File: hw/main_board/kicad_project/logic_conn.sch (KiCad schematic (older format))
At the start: 11 parts, among them P6 CONN_20X2, U8 MAX3002, U9 MAX3002

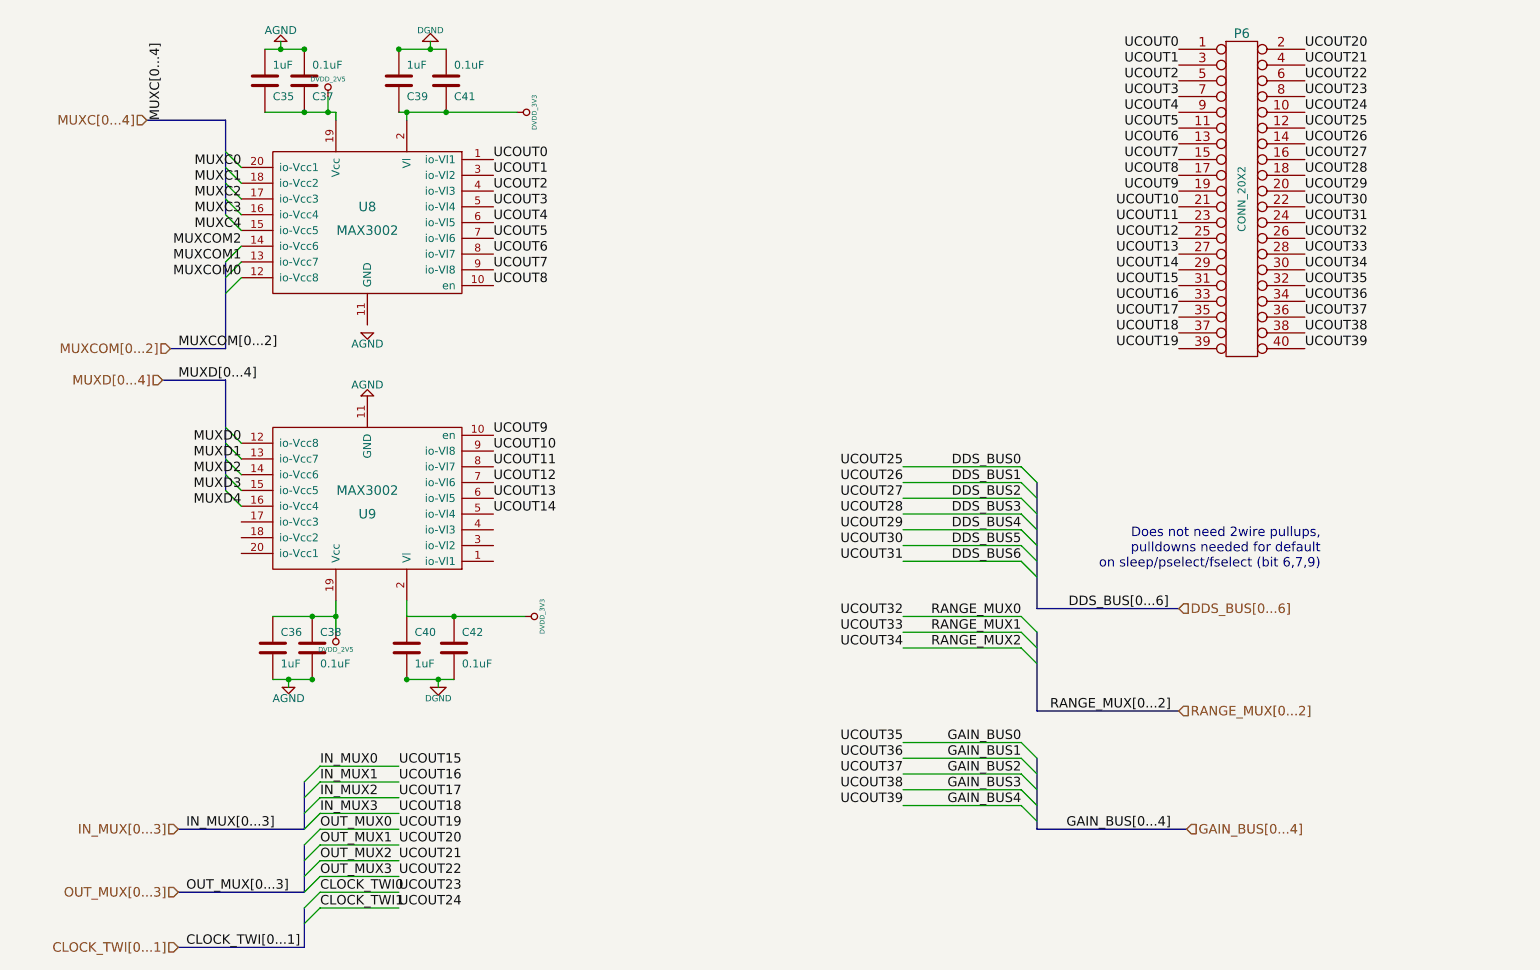
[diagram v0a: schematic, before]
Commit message: refactored schematic, finalized gain/range
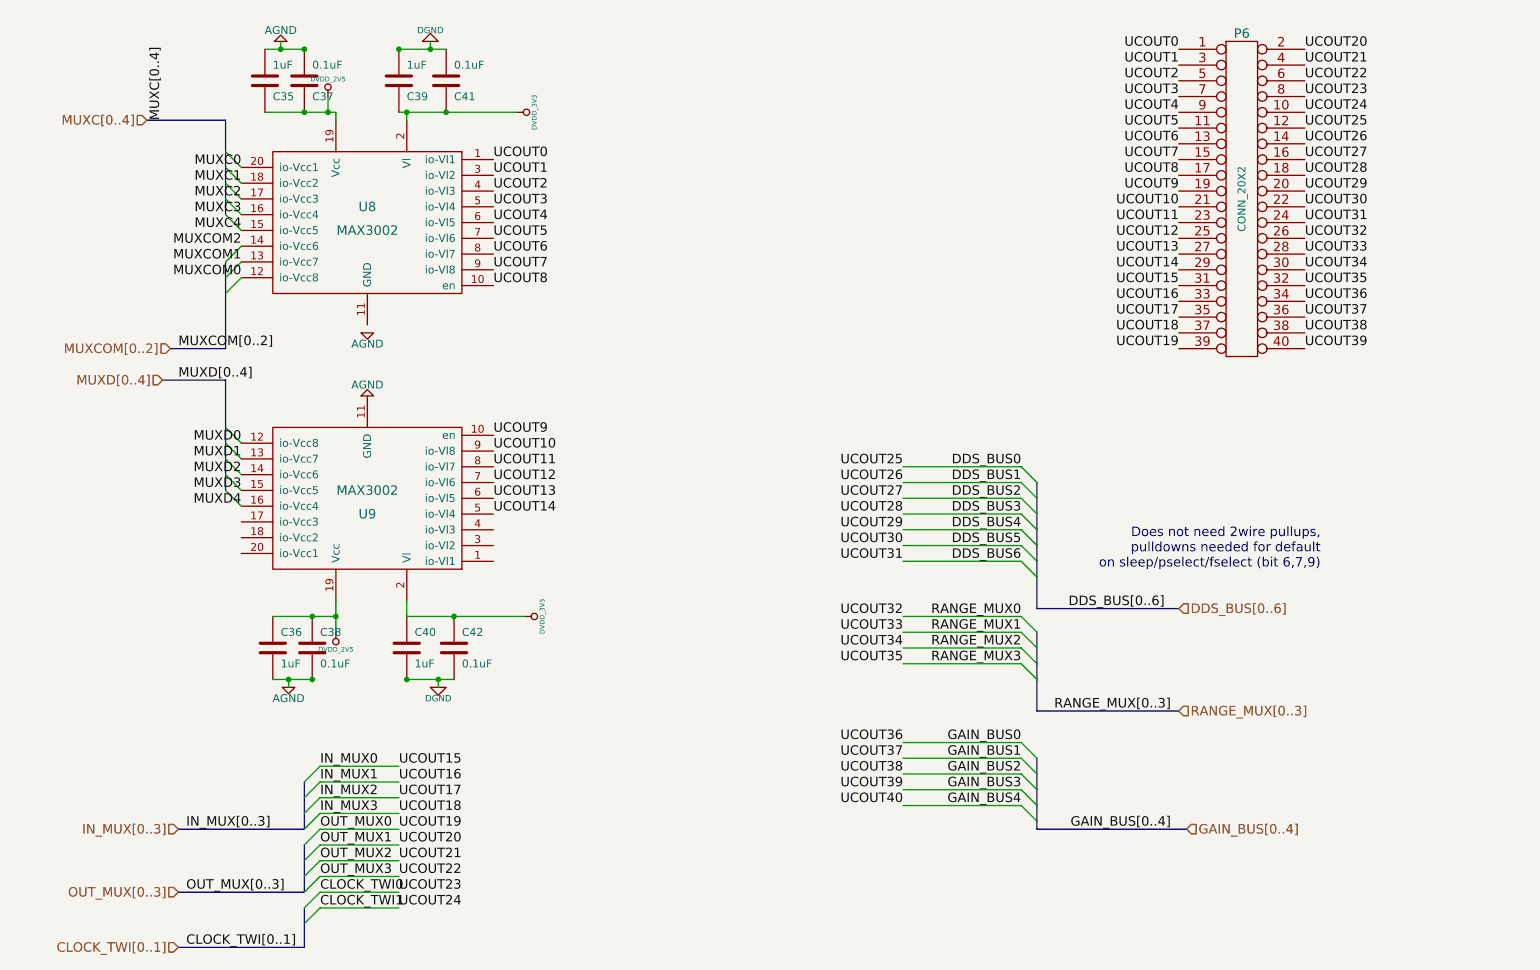
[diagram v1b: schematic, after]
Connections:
- net GAIN_BUS0: now also P6.34 (P34); no longer P6.32 (P32)
- net GAIN_BUS1: now also P6.36 (P36); no longer P6.34 (P34)
- net GAIN_BUS2: now also P6.38 (P38); no longer P6.36 (P36)
- net GAIN_BUS3: now also P6.40 (P40); no longer P6.38 (P38)
- net GAIN_BUS4: no longer P6.40 (P40)
- new net RANGE_MUX3: P6.32 (P32)
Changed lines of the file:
@@
 $Descr A4 11693 8268
 encoding utf-8
-Sheet 3 3
+Sheet 3 7
 Title ""
 Date "26 feb 2014"
@@
 $EndDescr
 Text Label 6900 5400 2    60   ~ 0
+UCOUT40
+Text Label 6900 5300 2    60   ~ 0
 UCOUT39
-Text Label 6900 5300 2    60   ~ 0
+Text Label 6900 5200 2    60   ~ 0
 UCOUT38
-Text Label 6900 5200 2    60   ~ 0
+Text Label 6900 5100 2    60   ~ 0
 UCOUT37
-Text Label 6900 5100 2    60   ~ 0
+Text Label 6900 5000 2    60   ~ 0
 UCOUT36
-Text Label 6900 5000 2    60   ~ 0
-UCOUT35
 Text Label 7650 5400 2    60   ~ 0
 GAIN_BUS4
@@
 GAIN_BUS0
 Text Label 8600 5550 2    60   ~ 0
-GAIN_BUS[0...4]
+GAIN_BUS[0..4]
 Text Label 8600 4800 2    60   ~ 0
-RANGE_MUX[0...2]
+RANGE_MUX[0..3]
 Wire Wire Line
 	7650 5400 6900 5400
@@
 DDS_BUS0
 Text Label 7950 4150 0    60   ~ 0
-DDS_BUS[0...6]
+DDS_BUS[0..6]
 Entry Wire Line
 	7650 3850 7750 3950
@@
 	7650 3250 7750 3350
 Text Label 2350 6300 0    60   ~ 0
-CLOCK_TWI[0...1]
+CLOCK_TWI[0..1]
 Text Label 2350 5950 0    60   ~ 0
-OUT_MUX[0...3]
+OUT_MUX[0..3]
 Text Label 3700 6050 0    60   ~ 0
 UCOUT24
@@
 IN_MUX0
 Text Label 2350 5550 0    60   ~ 0
-IN_MUX[0...3]
+IN_MUX[0..3]
 Entry Wire Line
 	3100 5450 3200 5350
@@
 UCOUT0
 Text Label 2300 2700 0    60   ~ 0
-MUXD[0...4]
+MUXD[0..4]
 Entry Wire Line
 	2600 3400 2700 3500
@@
 $EndComp
 Text Label 2300 2500 0    60   ~ 0
-MUXCOM[0...2]
+MUXCOM[0..2]
 Text Label 2200 1050 1    60   ~ 0
-MUXC[0...4]
+MUXC[0..4]
 $Comp
 L DVDD_3V3 #PWR047
@@
 Does not need 2wire pullups, \npulldowns needed for default\n on sleep/pselect/fselect (bit 6,7,9)
 Text HLabel 8650 4800 2    60   Input ~ 0
-RANGE_MUX[0...2]
+RANGE_MUX[0..3]
 Text HLabel 8700 5550 2    60   Input ~ 0
-GAIN_BUS[0...4]
+GAIN_BUS[0..4]
 Text HLabel 8650 4150 2    60   Input ~ 0
-DDS_BUS[0...6]
+DDS_BUS[0..6]
 Text HLabel 2300 5550 0    60   Input ~ 0
-IN_MUX[0...3]
+IN_MUX[0..3]
 Text HLabel 2300 5950 0    60   Input ~ 0
-OUT_MUX[0...3]
+OUT_MUX[0..3]
 Text HLabel 2300 6300 0    60   Input ~ 0
-CLOCK_TWI[0...1]
+CLOCK_TWI[0..1]
 Text HLabel 2100 1050 0    60   Input ~ 0
-MUXC[0...4]
+MUXC[0..4]
 Text HLabel 2250 2500 0    60   Input ~ 0
-MUXCOM[0...2]
+MUXCOM[0..2]
 Text HLabel 2200 2700 0    60   Input ~ 0
-MUXD[0...4]
+MUXD[0..4]
 $Comp
 L CONN_20X2 P6
@@
 Text Label 9450 2500 0    60   ~ 0
 UCOUT39
+Entry Wire Line
+	7650 4500 7750 4600
+Wire Wire Line
+	7650 4500 6900 4500
+Text Label 6900 4500 2    60   ~ 0
+UCOUT35
+Text Label 7650 4500 2    60   ~ 0
+RANGE_MUX3
 $EndSCHEMATC

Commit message: started mainboard pcb layout, fixing small things in schematic, TODO: schematic connector symbols and pads
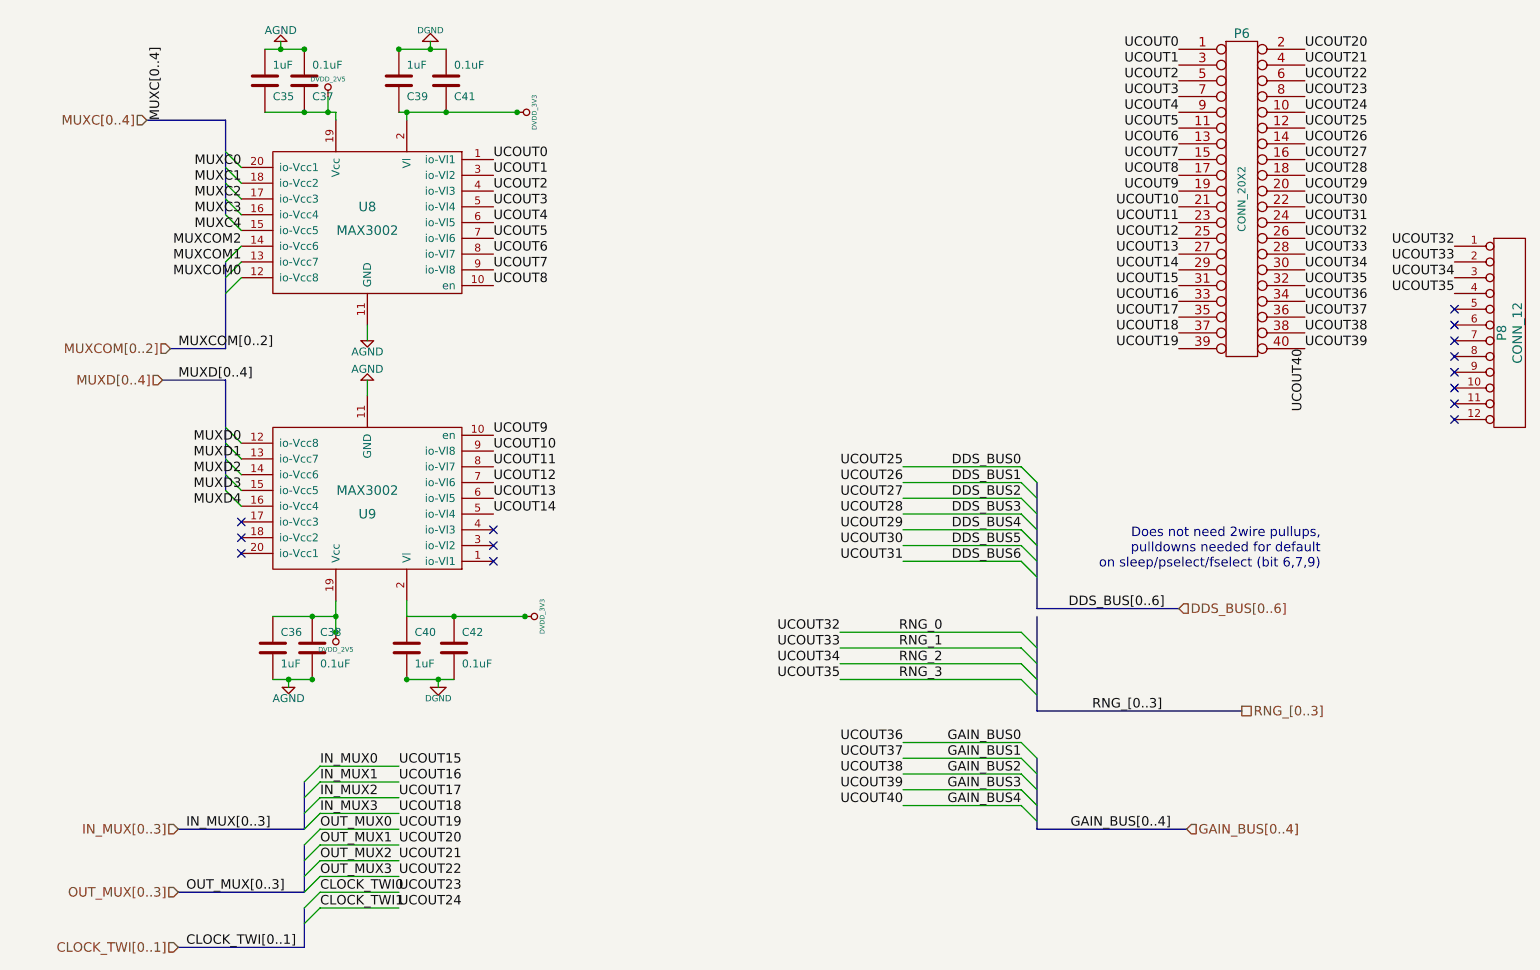
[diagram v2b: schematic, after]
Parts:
- added P8: CONN_12, symbol CONN_12
- C35, C36, C37, C38, C39, C40, C41, C42: footprint (none) -> 0603
- U8, U9: footprint (none) -> TSSOP_20
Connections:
- net AGND: now also U8.11 (GND)
- net RANGE_MUX0 renamed RNG_0
- net RNG_0: now also P8.1 (P1)
- net RANGE_MUX1 renamed RNG_1
- net RNG_1: now also P8.2 (P2)
- net RANGE_MUX2 renamed RNG_2
- net RNG_2: now also P8.3 (P3)
- net RANGE_MUX3 renamed RNG_3
- net RNG_3: now also P8.4 (P4)
- no-connect marks 0 -> 14
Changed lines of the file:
@@
 encoding utf-8
 Sheet 3 7
-Title ""
-Date "26 feb 2014"
-Rev ""
+Title "Microcontroller interface/translator"
+Date "01 Feb 2014"
+Rev "A"
 Comp ""
-Comment1 ""
+Comment1 "Copyright 2014 Andrey Shmakov"
 Comment2 ""
 Comment3 ""
@@
 Text Label 8600 5550 2    60   ~ 0
 GAIN_BUS[0..4]
-Text Label 8600 4800 2    60   ~ 0
-RANGE_MUX[0..3]
 Wire Wire Line
 	7650 5400 6900 5400
@@
 Wire Wire Line
 	7650 5000 6900 5000
-Wire Wire Line
-	7650 4400 6900 4400
-Wire Wire Line
-	7650 4300 6900 4300
-Wire Wire Line
-	7650 4200 6900 4200
 Wire Wire Line
 	7650 3850 6900 3850
@@
 	7750 4150 7750 3350
 Wire Bus Line
-	8650 4800 7750 4800
-Wire Bus Line
-	7750 4800 7750 4300
-Wire Bus Line
 	8700 5550 7750 5550
 Wire Bus Line
@@
 Entry Wire Line
 	7650 5000 7750 5100
-Text Label 7650 4400 2    60   ~ 0
-RANGE_MUX2
-Text Label 7650 4300 2    60   ~ 0
-RANGE_MUX1
-Text Label 7650 4200 2    60   ~ 0
-RANGE_MUX0
-Text Label 6900 4400 2    60   ~ 0
-UCOUT34
-Text Label 6900 4300 2    60   ~ 0
-UCOUT33
-Text Label 6900 4200 2    60   ~ 0
-UCOUT32
-Entry Wire Line
-	7650 4400 7750 4500
-Entry Wire Line
-	7650 4300 7750 4400
-Entry Wire Line
-	7650 4200 7750 4300
 Text Label 6900 3850 2    60   ~ 0
 UCOUT31
@@
 F 0 "U9" H 3500 3550 60  0000 C CNN
 F 1 "MAX3002" H 3500 3400 60  0000 C CNN
-F 2 "" H 3500 3450 60  0001 C CNN
+F 2 "TSSOP_20" H 3500 3450 60  0001 C CNN
 F 3 "" H 3500 3450 60  0001 C CNN
 	1    3500 3450
@@
 $EndComp
 $Comp
-L DVDD_2V5 #PWR042
+L DVDD_2V5 #PWR08
 U 1 1 5245D941
 P 3300 4300
-F 0 "#PWR042" H 3300 4400 30  0001 C CNN
+F 0 "#PWR08" H 3300 4400 30  0001 C CNN
 F 1 "DVDD_2V5" H 3300 4410 30  0000 C CNN
 F 2 "" H 3300 4300 60  0001 C CNN
@@
 F 0 "C38" H 3200 4500 50  0000 L CNN
 F 1 "0.1uF" H 3200 4300 50  0000 L CNN
-F 2 "" H 3150 4400 60  0001 C CNN
+F 2 "0603" H 3150 4400 60  0001 C CNN
 F 3 "" H 3150 4400 60  0001 C CNN
 	1    3150 4400
@@
 F 0 "C36" H 2950 4500 50  0000 L CNN
 F 1 "1uF" H 2950 4300 50  0000 L CNN
-F 2 "" H 2900 4400 60  0001 C CNN
+F 2 "0603" H 2900 4400 60  0001 C CNN
 F 3 "" H 2900 4400 60  0001 C CNN
 	1    2900 4400
@@
 F 0 "C42" H 4100 4500 50  0000 L CNN
 F 1 "0.1uF" H 4100 4300 50  0000 L CNN
-F 2 "" H 4050 4400 60  0001 C CNN
+F 2 "0603" H 4050 4400 60  0001 C CNN
 F 3 "" H 4050 4400 60  0001 C CNN
 	1    4050 4400
@@
 F 0 "C40" H 3800 4500 50  0000 L CNN
 F 1 "1uF" H 3800 4300 50  0000 L CNN
-F 2 "" H 3750 4400 60  0001 C CNN
+F 2 "0603" H 3750 4400 60  0001 C CNN
 F 3 "" H 3750 4400 60  0001 C CNN
 	1    3750 4400
@@
 $EndComp
 $Comp
-L AGND #PWR043
+L AGND #PWR09
 U 1 1 5245D93C
 P 3000 4650
-F 0 "#PWR043" H 3000 4650 40  0001 C CNN
+F 0 "#PWR09" H 3000 4650 40  0001 C CNN
 F 1 "AGND" H 3000 4580 50  0000 C CNN
 F 2 "" H 3000 4650 60  0001 C CNN
@@
 $EndComp
 $Comp
-L DGND #PWR044
+L DGND #PWR010
 U 1 1 5245D93B
 P 3950 4650
-F 0 "#PWR044" H 3950 4650 40  0001 C CNN
+F 0 "#PWR010" H 3950 4650 40  0001 C CNN
 F 1 "DGND" H 3950 4580 40  0000 C CNN
 F 2 "" H 3950 4650 60  0001 C CNN
@@
 $EndComp
 $Comp
-L AGND #PWR045
+L AGND #PWR011
 U 1 1 5245D93A
-P 3500 2800
-F 0 "#PWR045" H 3500 2800 40  0001 C CNN
-F 1 "AGND" H 3500 2730 50  0000 C CNN
-F 2 "" H 3500 2800 60  0001 C CNN
-F 3 "" H 3500 2800 60  0001 C CNN
-	1    3500 2800
+P 3500 2700
+F 0 "#PWR011" H 3500 2700 40  0001 C CNN
+F 1 "AGND" H 3500 2630 50  0000 C CNN
+F 2 "" H 3500 2700 60  0001 C CNN
+F 3 "" H 3500 2700 60  0001 C CNN
+	1    3500 2700
 	1    0    0    1
 $EndComp
 $Comp
-L DVDD_3V3 #PWR046
+L DVDD_3V3 #PWR012
 U 1 1 5245D939
 P 4500 4200
-F 0 "#PWR046" H 4500 4300 30  0001 C CNN
+F 0 "#PWR012" H 4500 4300 30  0001 C CNN
 F 1 "DVDD_3V3" H 4500 4310 30  0000 C CNN
 F 2 "" H 4500 4200 60  0001 C CNN
@@
 MUXC[0..4]
 $Comp
-L DVDD_3V3 #PWR047
+L DVDD_3V3 #PWR013
 U 1 1 523C1EE9
 P 4450 1000
-F 0 "#PWR047" H 4450 1100 30  0001 C CNN
+F 0 "#PWR013" H 4450 1100 30  0001 C CNN
 F 1 "DVDD_3V3" H 4450 1110 30  0000 C CNN
 F 2 "" H 4450 1000 60  0001 C CNN
@@
 $EndComp
 $Comp
-L AGND #PWR048
+L AGND #PWR014
 U 1 1 523C1EBE
-P 3500 2400
-F 0 "#PWR048" H 3500 2400 40  0001 C CNN
-F 1 "AGND" H 3500 2330 50  0000 C CNN
-F 2 "" H 3500 2400 60  0001 C CNN
-F 3 "" H 3500 2400 60  0001 C CNN
-	1    3500 2400
-	1    0    0    -1
-$EndComp
-$Comp
-L DGND #PWR049
+P 3500 2450
+F 0 "#PWR014" H 3500 2450 40  0001 C CNN
+F 1 "AGND" H 3500 2380 50  0000 C CNN
+F 2 "" H 3500 2450 60  0001 C CNN
+F 3 "" H 3500 2450 60  0001 C CNN
+	1    3500 2450
+	1    0    0    -1
+$EndComp
+$Comp
+L DGND #PWR015
 U 1 1 523C1EBD
 P 3900 550
-F 0 "#PWR049" H 3900 550 40  0001 C CNN
+F 0 "#PWR015" H 3900 550 40  0001 C CNN
 F 1 "DGND" H 3900 480 40  0000 C CNN
 F 2 "" H 3900 550 60  0001 C CNN
@@
 $EndComp
 $Comp
-L AGND #PWR050
+L AGND #PWR016
 U 1 1 523C1EBC
 P 2950 550
-F 0 "#PWR050" H 2950 550 40  0001 C CNN
+F 0 "#PWR016" H 2950 550 40  0001 C CNN
 F 1 "AGND" H 2950 480 50  0000 C CNN
 F 2 "" H 2950 550 60  0001 C CNN
@@
 F 0 "C39" H 3750 900 50  0000 L CNN
 F 1 "1uF" H 3750 700 50  0000 L CNN
-F 2 "" H 3700 800 60  0001 C CNN
+F 2 "0603" H 3700 800 60  0001 C CNN
 F 3 "" H 3700 800 60  0001 C CNN
 	1    3700 800
@@
 F 0 "C41" H 4050 900 50  0000 L CNN
 F 1 "0.1uF" H 4050 700 50  0000 L CNN
-F 2 "" H 4000 800 60  0001 C CNN
+F 2 "0603" H 4000 800 60  0001 C CNN
 F 3 "" H 4000 800 60  0001 C CNN
 	1    4000 800
@@
 F 0 "C35" H 2900 900 50  0000 L CNN
 F 1 "1uF" H 2900 700 50  0000 L CNN
-F 2 "" H 2850 800 60  0001 C CNN
+F 2 "0603" H 2850 800 60  0001 C CNN
 F 3 "" H 2850 800 60  0001 C CNN
 	1    2850 800
@@
 F 0 "C37" H 3150 900 50  0000 L CNN
 F 1 "0.1uF" H 3150 700 50  0000 L CNN
-F 2 "" H 3100 800 60  0001 C CNN
+F 2 "0603" H 3100 800 60  0001 C CNN
 F 3 "" H 3100 800 60  0001 C CNN
 	1    3100 800
@@
 $EndComp
 $Comp
-L DVDD_2V5 #PWR051
+L DVDD_2V5 #PWR017
 U 1 1 523C1EB7
 P 3250 900
-F 0 "#PWR051" H 3250 1000 30  0001 C CNN
+F 0 "#PWR017" H 3250 1000 30  0001 C CNN
 F 1 "DVDD_2V5" H 3250 1010 30  0000 C CNN
 F 2 "" H 3250 900 60  0001 C CNN
@@
 F 0 "U8" H 3500 1800 60  0000 C CNN
 F 1 "MAX3002" H 3500 1650 60  0000 C CNN
-F 2 "" H 3500 1700 60  0001 C CNN
+F 2 "TSSOP_20" H 3500 1700 60  0001 C CNN
 F 3 "" H 3500 1700 60  0001 C CNN
 	1    3500 1700
@@
 Text Notes 9550 3900 2    60   ~ 0
 Does not need 2wire pullups, \npulldowns needed for default\n on sleep/pselect/fselect (bit 6,7,9)
-Text HLabel 8650 4800 2    60   Input ~ 0
-RANGE_MUX[0..3]
 Text HLabel 8700 5550 2    60   Input ~ 0
 GAIN_BUS[0..4]
@@
 Text HLabel 2200 2700 0    60   Input ~ 0
 MUXD[0..4]
-$Comp
-L CONN_20X2 P6
-U 1 1 530D6B88
-P 9050 1550
-F 0 "P6" H 9050 2600 60  0000 C CNN
-F 1 "CONN_20X2" V 9050 1550 50  0000 C CNN
-F 2 "" H 9050 1550 60  0000 C CNN
-F 3 "" H 9050 1550 60  0000 C CNN
-	1    9050 1550
-	1    0    0    -1
-$EndComp
 Text Label 8650 600  2    60   ~ 0
 UCOUT0
@@
 Text Label 9450 1700 0    60   ~ 0
 UCOUT31
+Text Label 9450 2200 0    60   ~ 0
+UCOUT36
+Text Label 9450 2300 0    60   ~ 0
+UCOUT37
+Text Label 9450 2400 0    60   ~ 0
+UCOUT38
+Text Label 9450 2500 0    60   ~ 0
+UCOUT39
+Text Label 9450 2500 3    60   ~ 0
+UCOUT40
+Wire Wire Line
+	3500 2450 3500 2350
+Wire Wire Line
+	3500 2800 3500 2700
+NoConn ~ 2700 3600
+NoConn ~ 2700 3700
+NoConn ~ 2700 3800
+NoConn ~ 4300 3650
+NoConn ~ 4300 3750
+NoConn ~ 4300 3850
+Connection ~ 3300 4300
+Connection ~ 4500 4200
+Connection ~ 4450 1000
+Text Label 6500 4300 2    60   ~ 0
+UCOUT32
+Text Label 6500 4400 2    60   ~ 0
+UCOUT33
+Text Label 6500 4500 2    60   ~ 0
+UCOUT34
+Text Label 6500 4600 2    60   ~ 0
+UCOUT35
+Wire Wire Line
+	6500 4300 7650 4300
+Wire Wire Line
+	6500 4400 7650 4400
+Wire Wire Line
+	6500 4500 7650 4500
+Wire Wire Line
+	6500 4600 7650 4600
+Entry Wire Line
+	7650 4300 7750 4400
+Entry Wire Line
+	7650 4400 7750 4500
+Entry Wire Line
+	7650 4500 7750 4600
+Entry Wire Line
+	7650 4600 7750 4700
+Wire Bus Line
+	7750 4200 7750 4800
+Wire Bus Line
+	7750 4800 9050 4800
+Text Label 8100 4800 0    60   ~ 0
+RNG_[0..3]
+Text HLabel 9050 4800 2    60   UnSpc ~ 0
+RNG_[0..3]
 Text Label 9450 1800 0    60   ~ 0
 UCOUT32
@@
 Text Label 9450 2100 0    60   ~ 0
 UCOUT35
-Text Label 9450 2200 0    60   ~ 0
-UCOUT36
-Text Label 9450 2300 0    60   ~ 0
-UCOUT37
-Text Label 9450 2400 0    60   ~ 0
-UCOUT38
-Text Label 9450 2500 0    60   ~ 0
-UCOUT39
-Entry Wire Line
-	7650 4500 7750 4600
-Wire Wire Line
-	7650 4500 6900 4500
-Text Label 6900 4500 2    60   ~ 0
+$Comp
+L CONN_20X2 P6
+U 1 1 53197612
+P 9050 1550
+F 0 "P6" H 9050 2600 60  0000 C CNN
+F 1 "CONN_20X2" V 9050 1550 50  0000 C CNN
+F 2 "" H 9050 1550 60  0000 C CNN
+F 3 "" H 9050 1550 60  0000 C CNN
+	1    9050 1550
+	1    0    0    -1
+$EndComp
+$Comp
+L CONN_12 P8
+U 1 1 53198391
+P 10750 2400
+F 0 "P8" V 10700 2400 60  0000 C CNN
+F 1 "CONN_12" V 10800 2400 60  0000 C CNN
+F 2 "" H 10750 2400 60  0000 C CNN
+F 3 "" H 10750 2400 60  0000 C CNN
+	1    10750 2400
+	1    0    0    -1
+$EndComp
+Text Label 10400 1850 2    60   ~ 0
+UCOUT32
+Text Label 10400 1950 2    60   ~ 0
+UCOUT33
+Text Label 10400 2050 2    60   ~ 0
+UCOUT34
+Text Label 10400 2150 2    60   ~ 0
 UCOUT35
-Text Label 7650 4500 2    60   ~ 0
-RANGE_MUX3
+NoConn ~ 10400 2250
+NoConn ~ 10400 2350
+NoConn ~ 10400 2450
+NoConn ~ 10400 2550
+NoConn ~ 10400 2650
+NoConn ~ 10400 2750
+NoConn ~ 10400 2850
+NoConn ~ 10400 2950
+Text Label 7150 4300 2    60   ~ 0
+RNG_0
+Text Label 7150 4400 2    60   ~ 0
+RNG_1
+Text Label 7150 4500 2    60   ~ 0
+RNG_2
+Text Label 7150 4600 2    60   ~ 0
+RNG_3
 $EndSCHEMATC
